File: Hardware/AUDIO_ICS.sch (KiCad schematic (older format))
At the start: 32 parts

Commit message: Changing to global labels/pages in progress
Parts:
- removed X?: 24.576 MHz, symbol CRYSTAL
- added X?: 24.576 MHz, symbol CRYSTAL_SMD
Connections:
- wire segments 175 -> 205
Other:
- note added: "From MCU\n(Control)"
- note added: "To DFE"
- note added: "To MCU\n(DFE Reset)"
- note added: "To MCU\n(Status)"
- note added: "To S/PDIF\n(Digital In)"
- note added: "To analog\ninputs"
- note added: "To mic\narray"

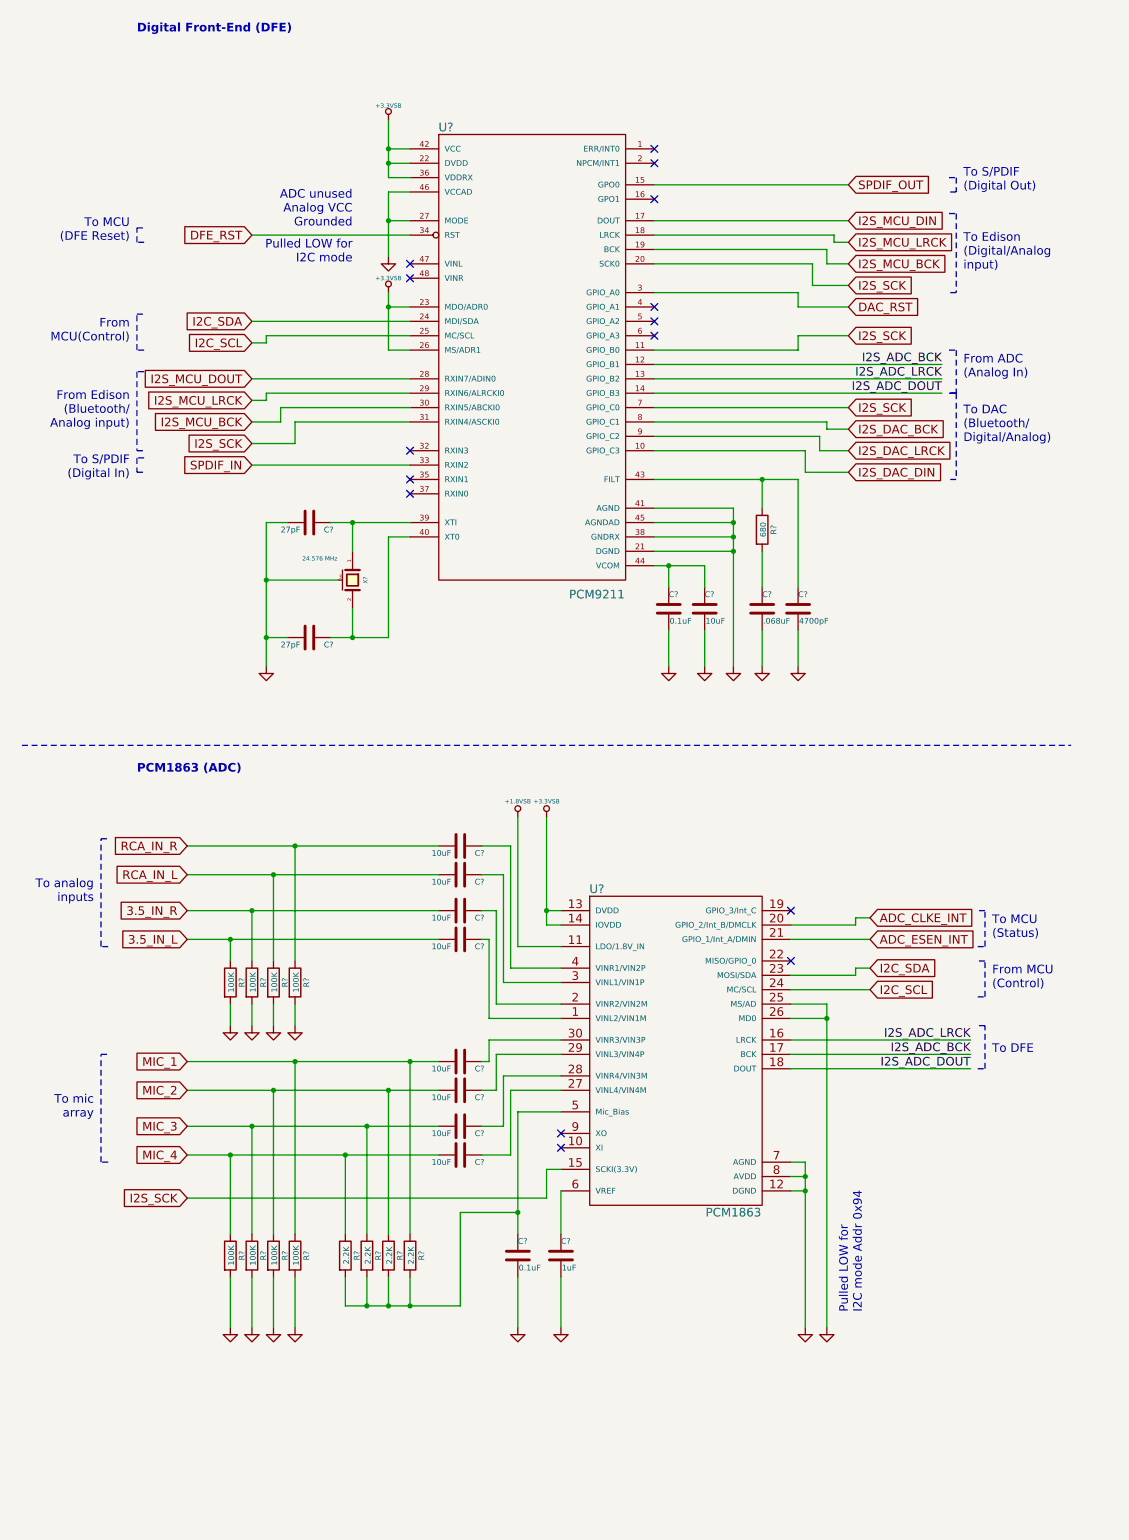
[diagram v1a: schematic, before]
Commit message: Finished converting to global labels
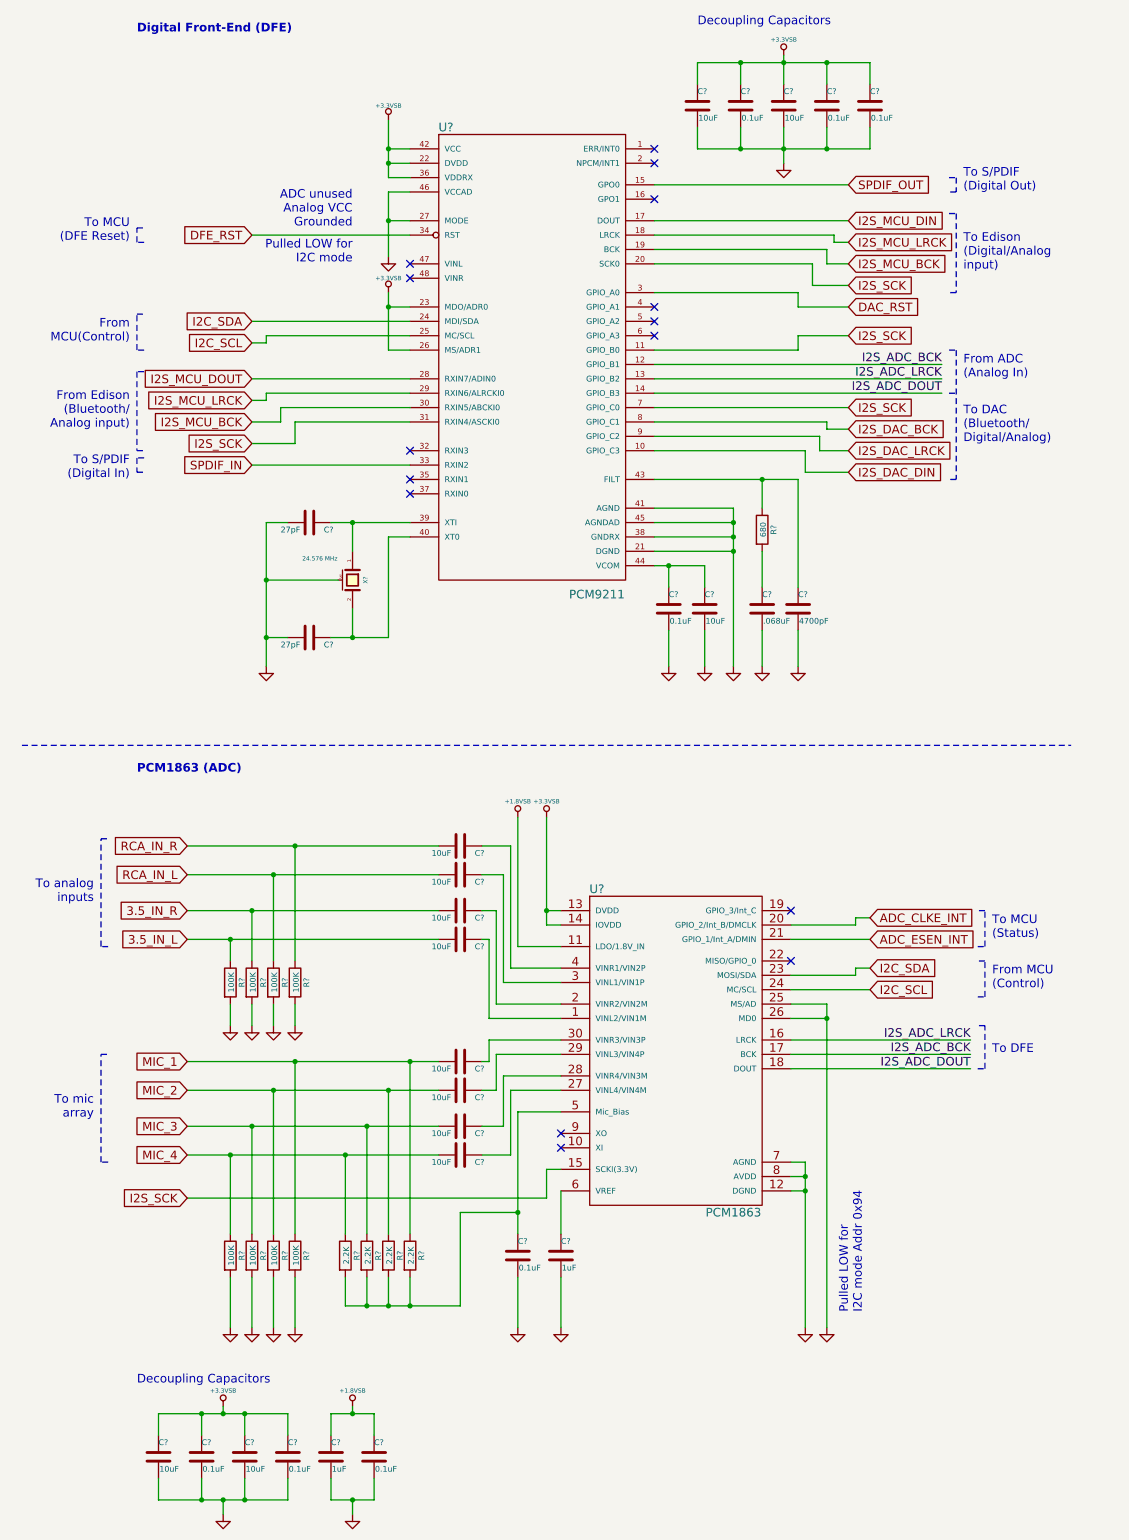
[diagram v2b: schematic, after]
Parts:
- added C? (x6): 0.1uF, symbol C-RESCUE-museV2
- added C?: 1uF, symbol C-RESCUE-museV2
- added C? (x4): 10uF, symbol C-RESCUE-museV2
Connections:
- net +1.8VSB: now also C?.1, C?.1
- net +3.3VSB: now also C?.1, C?.1, C?.1, C?.1, C?.1, C?.1, C?.1, C?.1, C?.1
- net GND: now also C?.2, C?.2, C?.2, C?.2, C?.2, C?.2, C?.2, C?.2, C?.2, C?.2, C?.2
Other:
- note added: "Decoupling Capacitors"

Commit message: Updated I2C pullup resistors and labels
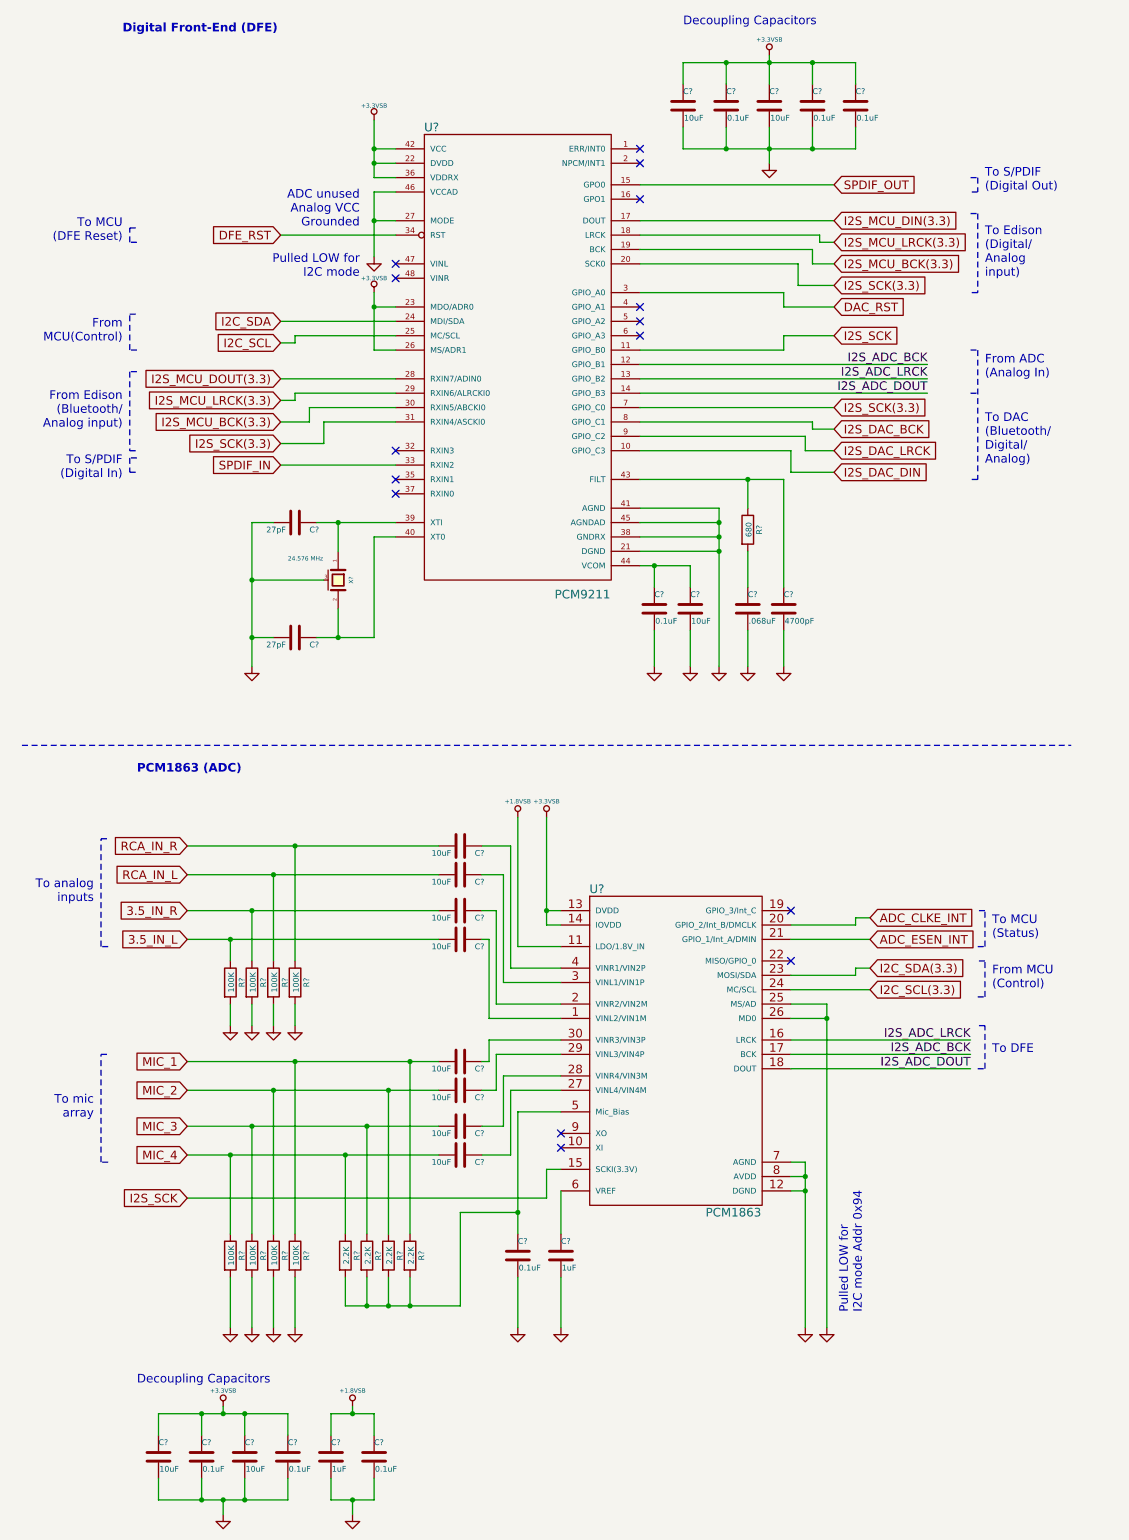
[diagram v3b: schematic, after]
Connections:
- net I2C_SCL: no longer U?.24 (MC/SCL)
- net I2C_SDA: no longer U?.23 (MOSI/SDA)
- net I2S_SCK: no longer U?.20 (SCK0), U?.31 (RXIN4/ASCKI0), U?.7 (GPIO_C0)
- net I2S_MCU_BCK renamed I2S_MCU_BCK(3.3)
- net I2S_MCU_DIN renamed I2S_MCU_DIN(3.3)
- net I2S_MCU_DOUT renamed I2S_MCU_DOUT(3.3)
- net I2S_MCU_LRCK renamed I2S_MCU_LRCK(3.3)
- new net I2C_SCL(3.3): U?.24 (MC/SCL)
- new net I2C_SDA(3.3): U?.23 (MOSI/SDA)
- new net I2S_SCK(3.3): U?.20 (SCK0), U?.31 (RXIN4/ASCKI0), U?.7 (GPIO_C0)
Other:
- note added: "To DAC\n(Bluetooth/\nDigital/\nAnalog)"
- note added: "To Edison\n(Digital/\nAnalog\ninput)"
- note removed: "To DAC\n(Bluetooth/\nDigital/Analog)"
- note removed: "To Edison\n(Digital/Analog\ninput)"
- moved on the sheet: C?, R?, U?, X?

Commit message: Made design review fixes, added breakouts
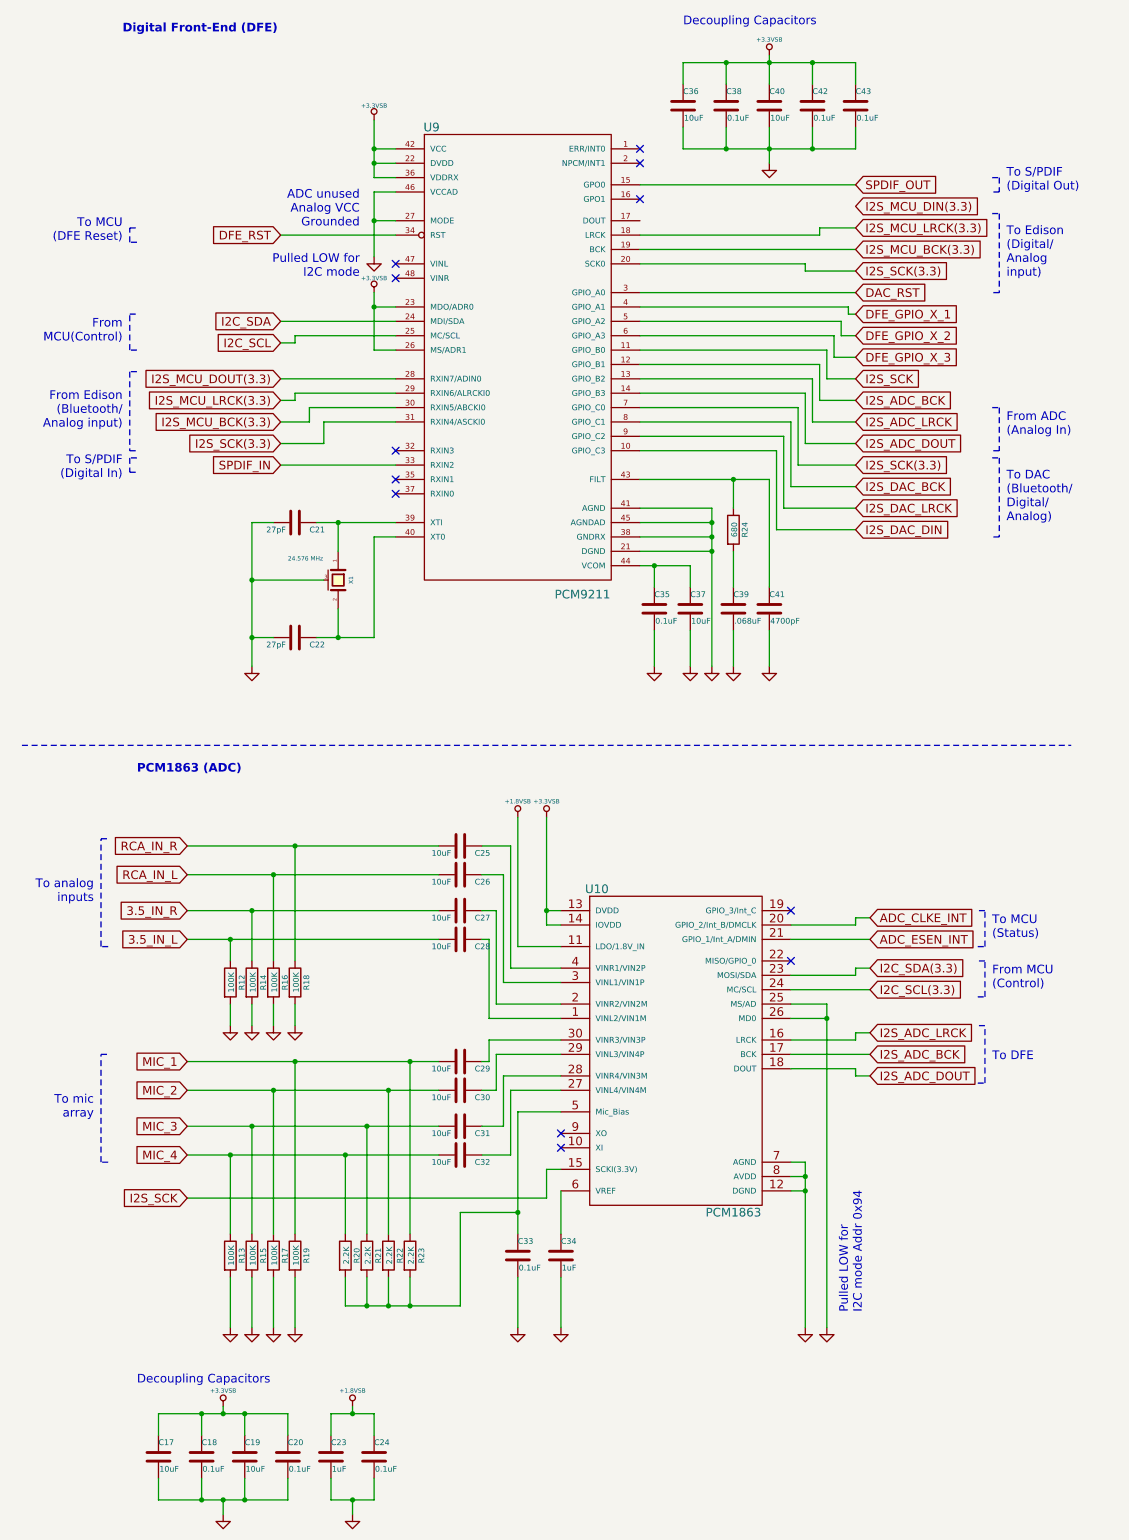
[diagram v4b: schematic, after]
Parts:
- gave numbers to parts that had none: 43
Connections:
- net I2S_MCU_DIN(3.3): no longer U9.17 (DOUT)
- net DFE_GPIO_X_1: now reaches U9.4 (GPIO_A1)
- net DFE_GPIO_X_2: now reaches U9.5 (GPIO_A2)
- net DFE_GPIO_X_3: now reaches U9.6 (GPIO_A3)
- no-connect marks 15 -> 12
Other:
- moved on the sheet: C39, C41, R24

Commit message: Annotated schematic
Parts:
- renumbered C36 to C15, C38 to C16, C40 to C17, C42 to C18, C43 to C19, C21 to C20, C35 to C21, C37 to C22, C39 to C23, C41 to C24, C22 to C25, C25 to C26, C26 to C27, C27 to C28, C28 to C29, C29 to C30, C30 to C31, C31 to C32, C32 to C33, C33 to C34, C34 to C35, C17 to C36, C18 to C37, C19 to C38, C20 to C39, C23 to C40, C24 to C41, R24 to R12, R12 to R13, R16 to R15, R18 to R16, R13 to R17, R15 to R18, R17 to R19, R19 to R20, R20 to R21, R21 to R22, R22 to R23, R23 to R24

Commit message: Annotation/Part Selection BOM Update
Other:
- moved on the sheet: C26, C27, C28, C29, C30, C31, C32, C33
